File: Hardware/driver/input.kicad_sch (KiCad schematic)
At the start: 55 parts, among them J301 1017526, Q301 IXTH80N075L2, Q302 IXTH80N075L2, U301 MCP3421A2T-ECH, U302 OPA2388, U303 DAC60501Z, U304 LM431SC, U305 MCP3421A3T-ECH, U306 OPA2388, U307 DAC60501Z, U308 LM431SC, U309 DS18B20, U310 DS18B20

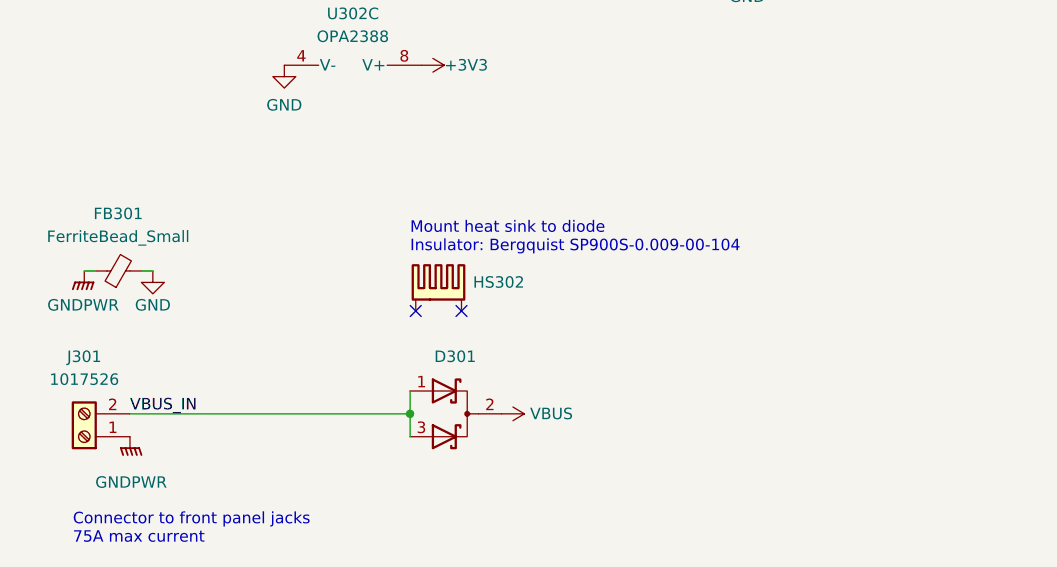
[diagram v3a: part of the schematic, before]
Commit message: Replaced load input connector
- Switched out the screw terminal for a pair of PCB mount studs, which
  then accept the wires from the front panel (with crimped hook or loop
  ferrules) and an associated nut.

  This gives way more clearance for a fan so hopefully a big high
  velocity one can fit.

- Moved input protection diodes up some more
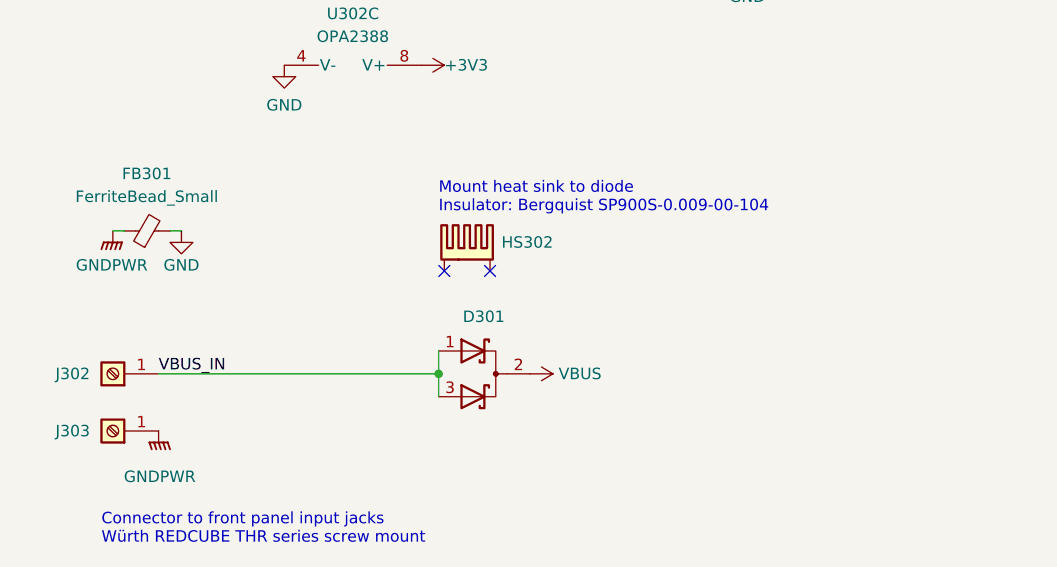
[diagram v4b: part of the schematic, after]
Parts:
- removed J301: 1017526, programmable-load:Phoenix-TDPT-2,1017526, symbol Connector:Screw_Terminal_01x02
- added J302, J303: Würth 74651194R, programmable-load:WE-74651194, symbol Connector:Screw_Terminal_01x01
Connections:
- net GNDPWR: now also J303.1 (Pin_1)
- net VBUS_IN: now also J302.1 (Pin_1)
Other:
- note added: "Connector to front panel input jacks Würth REDCUBE THR series screw mount"
- note removed: "Connector to front panel jacks 75A max current"
- moved on the sheet: D301, FB301, HS302

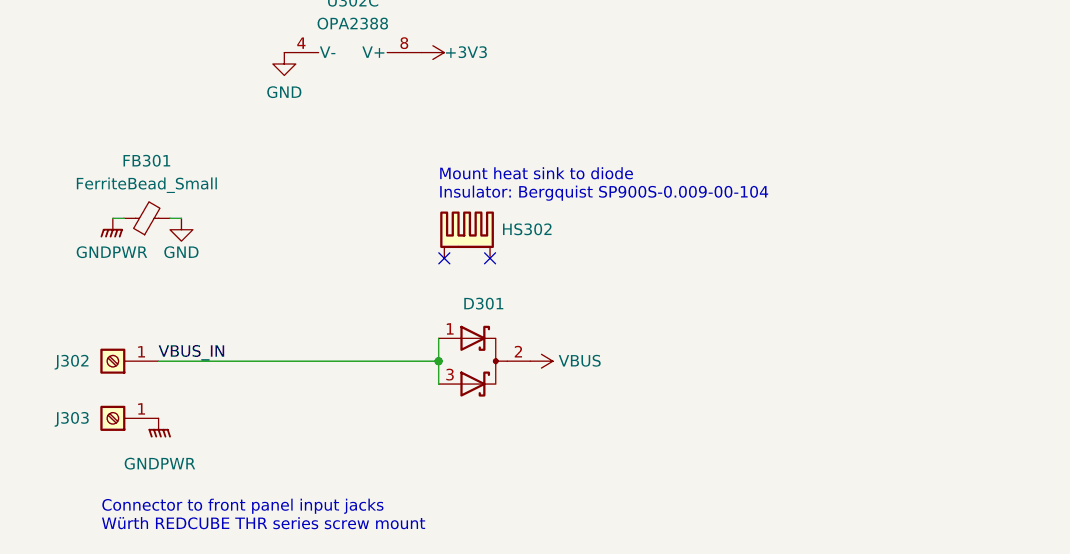
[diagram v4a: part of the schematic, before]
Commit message: Added some more protection to driver input
- Placed an overvoltage protection diode (TVS) at the input of the load
  driver board, and moved some more stuff around in preparation for
  manufacturing
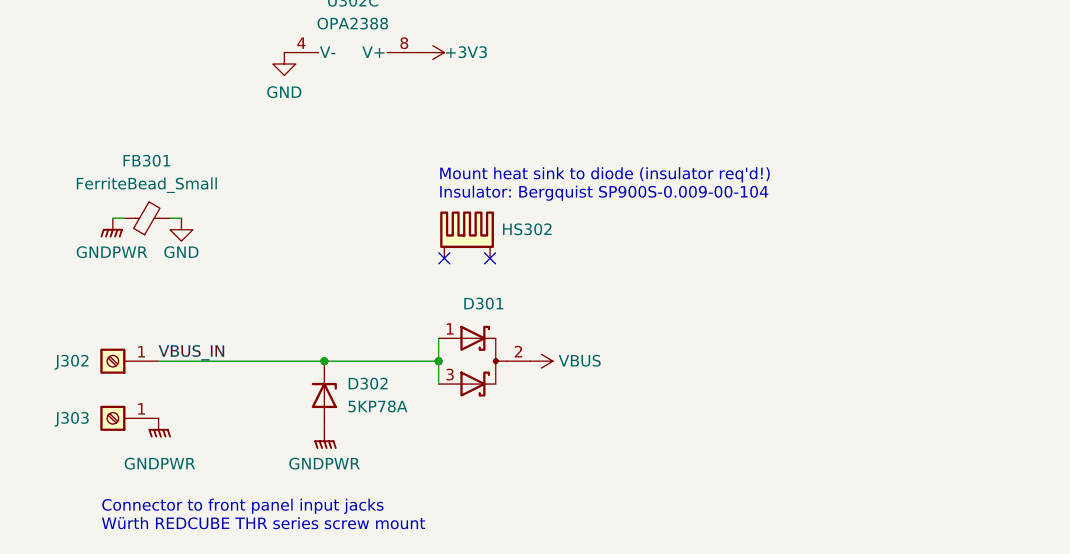
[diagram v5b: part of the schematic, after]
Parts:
- added D302: 5KP78A, Diode_THT:D_P600_R-6_P20.00mm_Horizontal, symbol Diode:5KPxxA
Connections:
- net GNDPWR: now also D302.2 (A2)
- net VBUS_IN: now also D302.1 (A1)
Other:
- note added: "Mount heat sink to diode (insulator req'd!) Insulator: Bergquist SP900S-0.009-00-104"
- note removed: "Mount heat sink to diode Insulator: Bergquist SP900S-0.009-00-104"
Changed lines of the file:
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@@
   (junction (at 155.575 122.555) (diameter 0) (color 0 0 0 0)
+  )
+  (junction (at 46.99 174.625) (diameter 0) (color 0 0 0 0)
   )
   (junction (at 111.76 53.975) (diameter 0) (color 0 0 0 0)
@@
     (stroke (width 0) (type default) (color 0 0 0 0))
   )
+  (wire (pts (xy 46.99 174.625) (xy 59.69 174.625))
+    (stroke (width 0) (type default) (color 0 0 0 0))
+  )
   (wire (pts (xy 92.71 22.86) (xy 83.82 22.86))
     (stroke (width 0) (type default) (color 0 0 0 0))
@@
     (stroke (width 0) (type default) (color 0 0 0 0))
   )
-  (wire (pts (xy 28.575 174.625) (xy 59.69 174.625))
+  (wire (pts (xy 28.575 174.625) (xy 46.99 174.625))
     (stroke (width 0) (type default) (color 0 0 0 0))
   )
@@
     (effects (font (size 1.27 1.27)) (justify left bottom))
   )
-  (text "Mount heat sink to diode\nInsulator: Bergquist SP900S-0.009-00-104"
+  (text "Mount heat sink to diode (insulator req'd!)\nInsulator: Bergquist SP900S-0.009-00-104"
     (at 59.69 156.845 0)
     (effects (font (size 1.27 1.27)) (justify left bottom))
@@
     (pin "2")
   )
+  (symbol (lib_id "power:GNDPWR") (at 46.99 182.245 0) (mirror y) (unit 1)
+    (in_bom yes) (on_board yes)
+    (property "Reference" "#PWR0126" (id 0) (at 46.99 187.325 0)
+      (effects (font (size 1.27 1.27)) hide)
+    )
+    (property "Value" "GNDPWR" (id 1) (at 46.99 186.055 0))
+    (property "Footprint" "" (id 2) (at 46.99 183.515 0)
+      (effects (font (size 1.27 1.27)) hide)
+    )
+    (property "Datasheet" "" (id 3) (at 46.99 183.515 0)
+      (effects (font (size 1.27 1.27)) hide)
+    )
+    (pin "1")
+  )
   (symbol (lib_id "power:GNDPWR") (at 31.75 40.64 0) (mirror y) (unit 1)
     (in_bom yes) (on_board yes)
@@
     (pin "1")
   )
+  (symbol (lib_id "Diode:5KPxxA") (at 46.99 178.435 270) (unit 1)
+    (in_bom yes) (on_board yes) (fields_autoplaced)
+    (property "Reference" "D302" (id 0) (at 49.53 177.1649 90)
+      (effects (font (size 1.27 1.27)) (justify left))
+    )
+    (property "Value" "5KP78A" (id 1) (at 49.53 179.7049 90)
+      (effects (font (size 1.27 1.27)) (justify left))
+    )
+    (property "Footprint" "Diode_THT:D_P600_R-6_P20.00mm_Horizontal" (id 2) (at 41.91 178.435 0)
+      (effects (font (size 1.27 1.27)) hide)
+    )
+    (property "Datasheet" "https://diotec.com/tl_files/diotec/files/pdf/datasheets/5kp65.pdf" (id 3) (at 46.99 177.165 0)
+      (effects (font (size 1.27 1.27)) hide)
+    )
+    (property "MPN" "5KP78A" (id 4) (at 46.99 178.435 90)
+      (effects (font (size 1.27 1.27)) hide)
+    )
+    (pin "1")
+    (pin "2")
+  )
   (symbol (lib_id "Device:R_Small") (at 48.26 25.4 90) (unit 1)

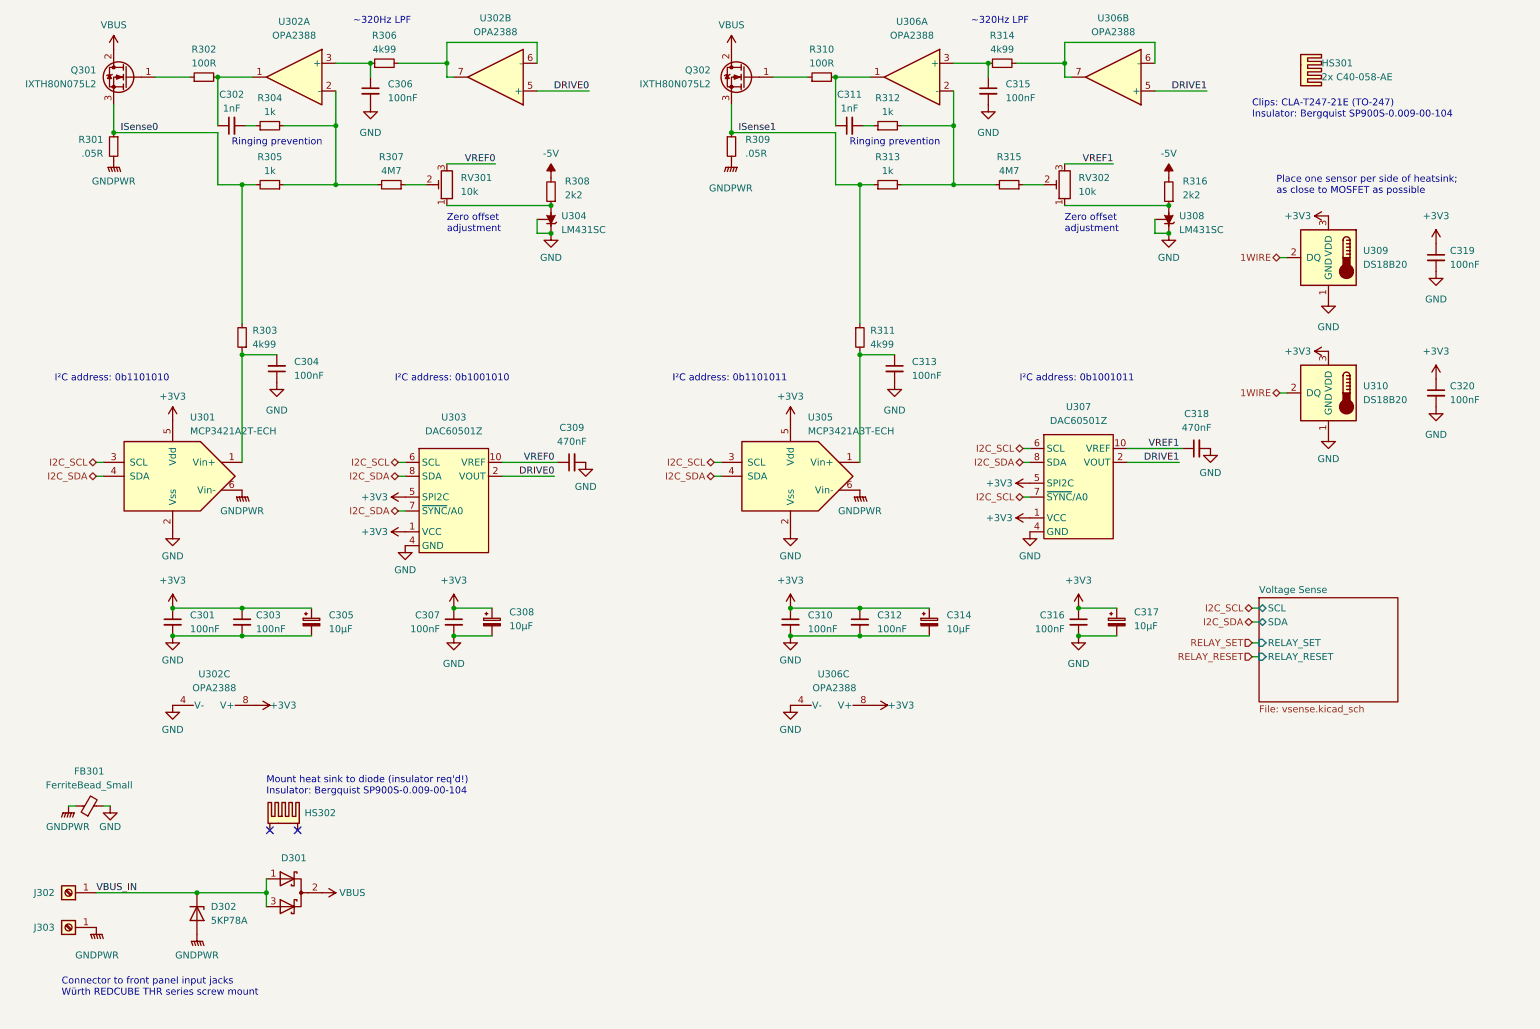
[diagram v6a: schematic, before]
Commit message: More rev 2 driver board work
- Updated power supply section with linear regulators for the +12V and
  +5V rails

- Replaced op amps for driving the MOSFETs with different ones, and
  updated them so that they actually run off the 12V rail instead of the
  3V3 rail.
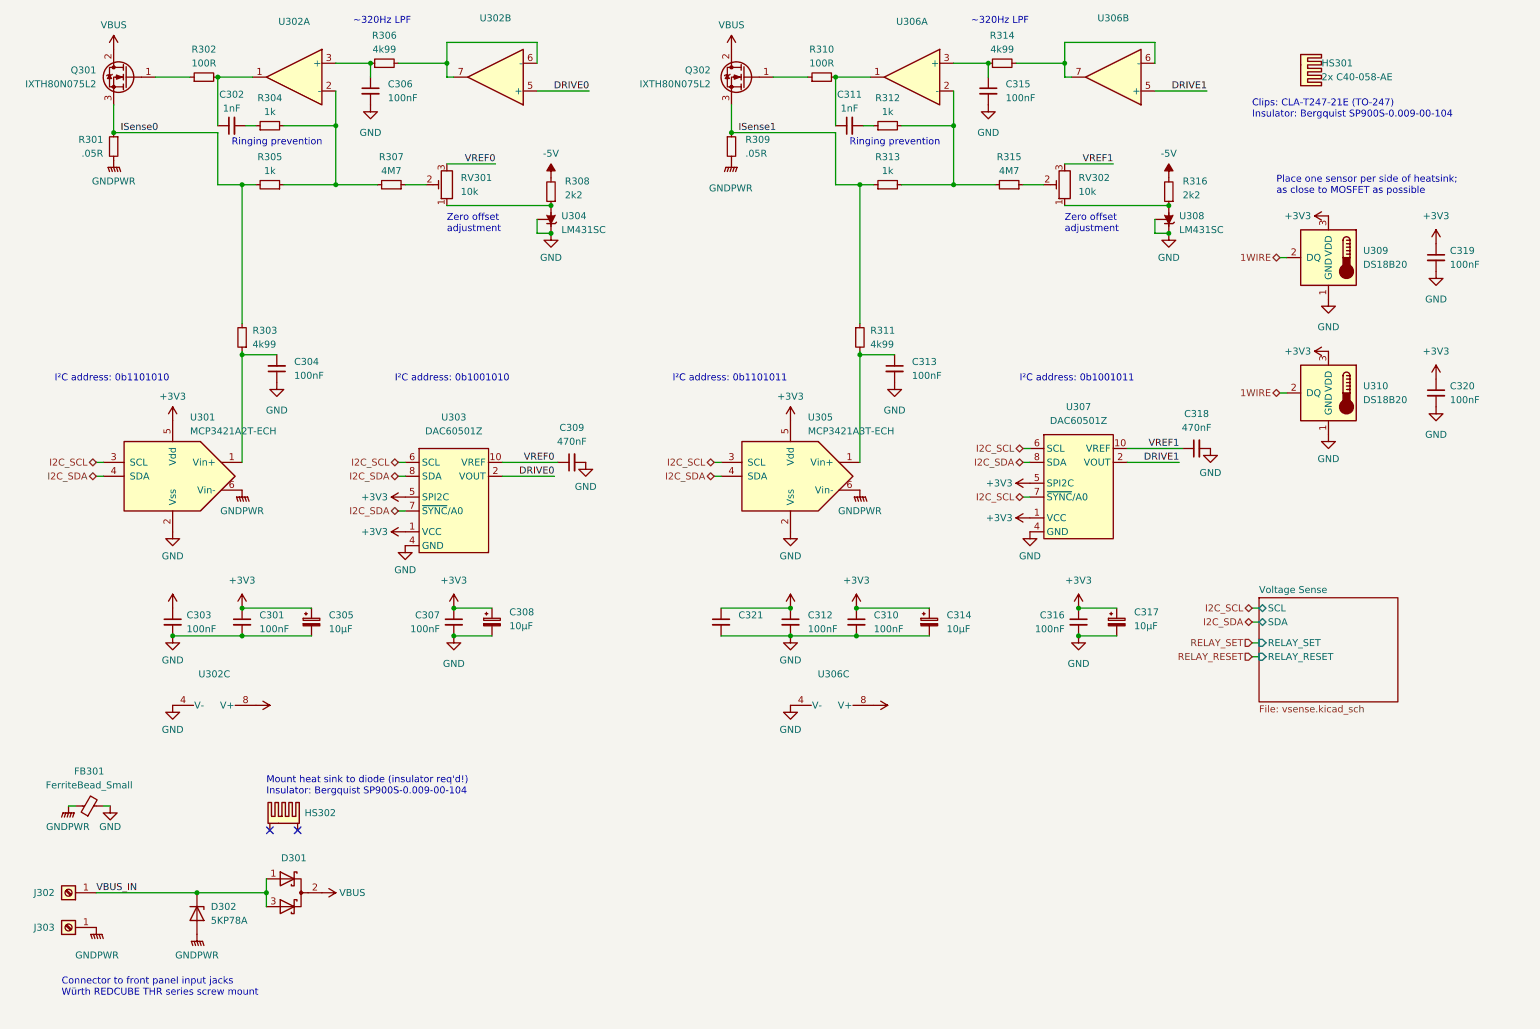
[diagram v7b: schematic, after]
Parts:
- added C321: (no value), symbol Device:C_Small
- U302, U306: value OPA2388 -> (none); footprint Package_SO:SOIC-8_3.9x4.9mm_P1.27mm -> (none); symbol programmable-load:OPA2388 -> programmable-load:ADA4522-2R; MPN OPA2388IDR -> ADA4522-2ARZ
- U302, U306: value OPA2388 -> (none); footprint Package_SO:SOIC-8_3.9x4.9mm_P1.27mm -> (none); symbol programmable-load:OPA2388 -> programmable-load:ADA4522-2R; MPN (none) -> ADA4522-2ARZ
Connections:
- net +3V3: no longer C303.1, C312.1, U302.8 (V+), U306.8 (V+)
- net GND: now also C321.2
- new net +12V: C303.1, C312.1, C321.1, U302.8 (V+), U306.8 (V+)
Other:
- moved on the sheet: C301, C303, C310, C312
